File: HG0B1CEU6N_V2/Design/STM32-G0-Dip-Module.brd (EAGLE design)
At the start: 51.1 x 22.7 mm, 35 parts, among them U1 STM32G0B1CEU6QFN_B1CEU6_STM-L, U2 TPS76433DBVT, X1 XTALL_CSTCE8M00G52

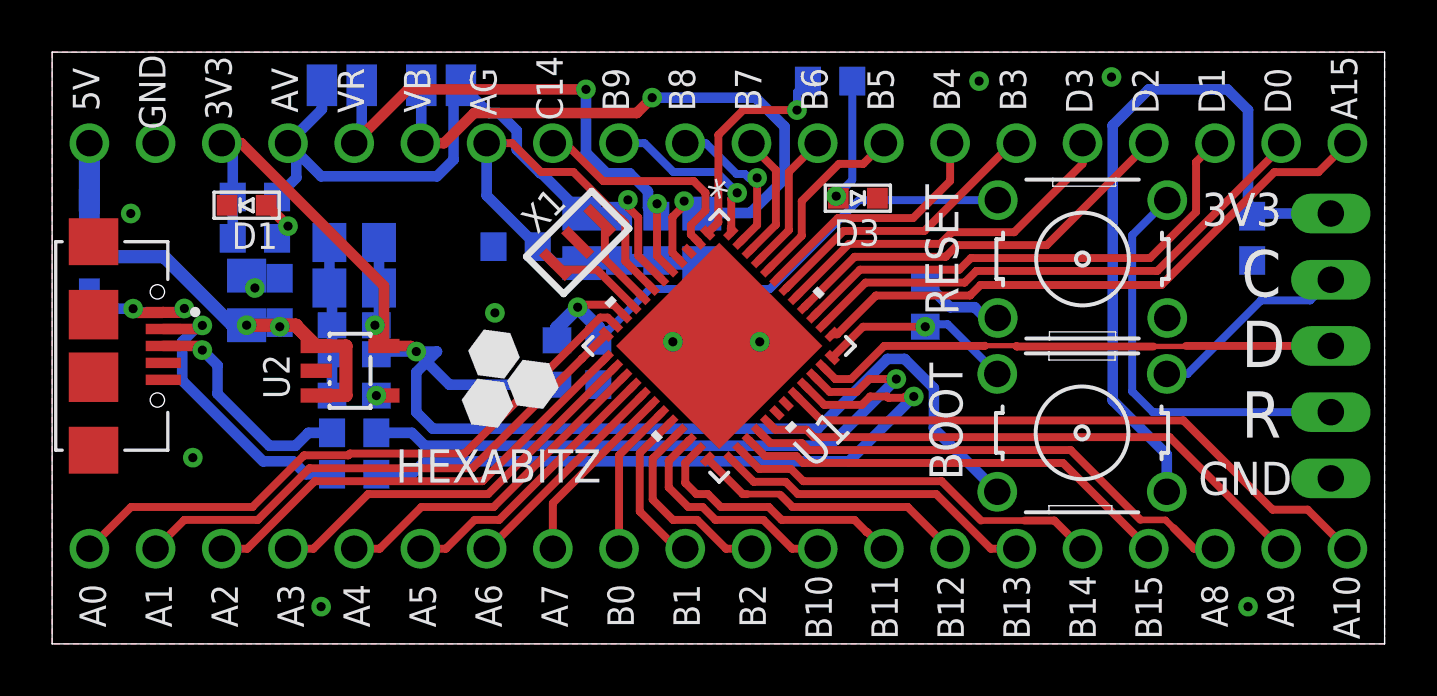
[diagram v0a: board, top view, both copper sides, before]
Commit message: -- Repairing some issues in the layout that related to keepout margins of the parts
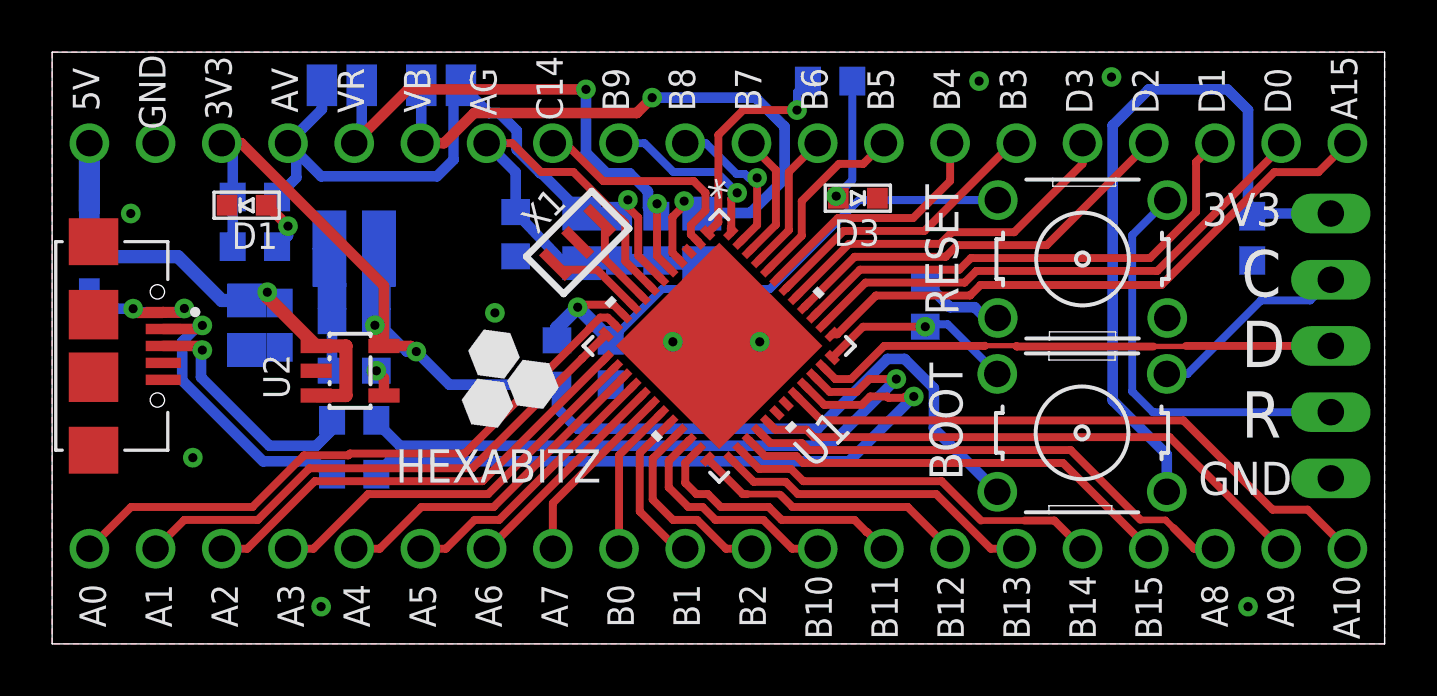
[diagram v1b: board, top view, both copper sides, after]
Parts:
- moved C12 1.27 mm to (-14.0, 12.4)
- moved C14 1.11 mm to (-14.0, 13.3)
- moved C3 0.95 mm to (-16.8, 12.2), turned to 270 degrees
- moved C7 0.95 mm to (-18.1, 12.2), turned to 270 degrees
- moved C8 0.95 mm to (-14.0, 10.5)
- moved C9 0.79 mm to (-14.0, 14.4)
- moved C10 0.48 mm to (-14.0, 15.9)
- moved R2 0.48 mm to (-7.78, 15.7), turned to 90 degrees
- moved R5 0.48 mm to (-14.0, 8.57)
- moved C16 0.48 mm to (-4.13, 10.8)
- moved R1 0.32 mm to (-17.8, 15.2)
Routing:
- net VDD: track 87.0 -> 80.2 mm
- net +5V: track 21.9 -> 19.7 mm, vias 2 -> 1
- net N$9: track 0.29 -> 1.07 mm
- net GND: track 9.26 -> 8.79 mm, vias 10 -> 9
